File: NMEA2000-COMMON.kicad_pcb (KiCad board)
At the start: 2 copper layers, 100 x 85 mm, 62 parts, among them J2 CAN, SW1 PRG, SW2 INSTANCE, SW3 BUS, U1 MCP2551-I-P, U2 TMR-2-2411, U3 74HCT595, U4 74HCT595, U5 Teensy_4.0

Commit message: Update silk layer.
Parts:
- moved TEST 5V0 0.06 mm to (23.2, 52.3)
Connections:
- TEST 5V0 pad 1: (no net) -> +3V3
- U5 pad 26: /3V3 -> +3V3
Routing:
- net /3V3: track 50.6 -> 0.00 mm
- net +3V3: track 0.00 -> 50.6 mm
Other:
- board text added: "TERMINATE BUS"
- board text removed: "TERMINATE BUS (120R)"

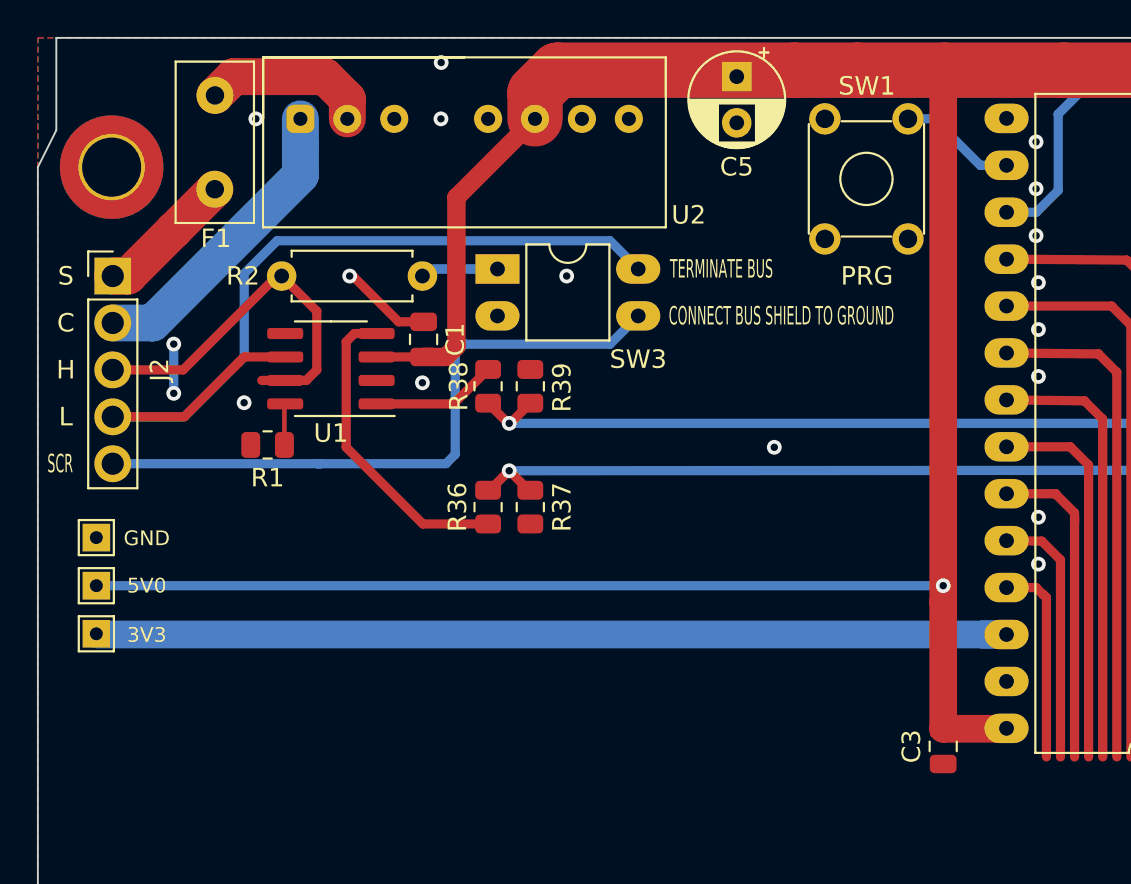
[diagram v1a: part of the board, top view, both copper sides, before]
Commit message: Update PRG switch position
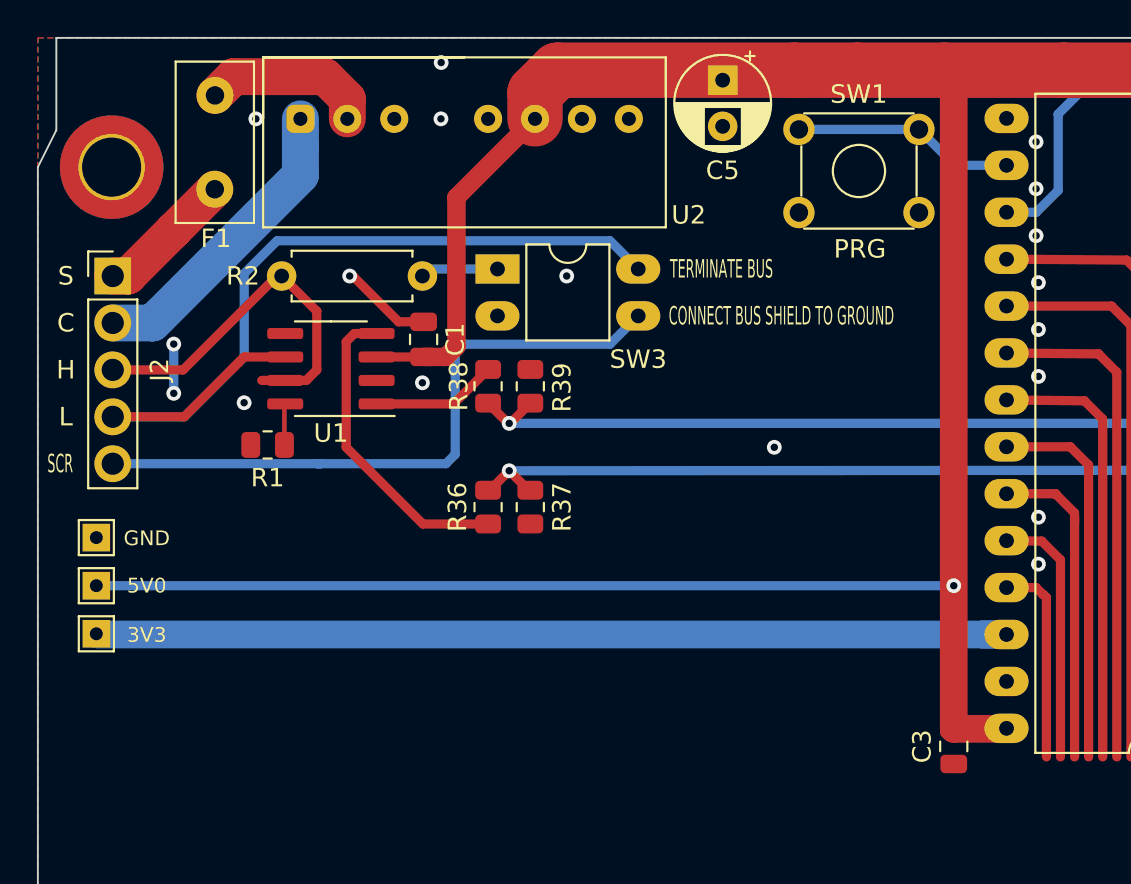
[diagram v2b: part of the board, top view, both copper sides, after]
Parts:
- moved SW1 5.93 mm to (61.2, 25.0), turned to 0 degrees
- moved C5 0.79 mm to (57.1, 22.3)
- moved C3 0.57 mm to (69.6, 58.4)
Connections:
- SW1 pad 2: Net-(SW1-Pad2) -> /PRG
- SW1 pad 4: Net-(SW1-Pad4) -> GND
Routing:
- net /PRG: track 6.35 -> 12.0 mm
